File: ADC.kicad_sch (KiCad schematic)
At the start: 32 parts, among them U107 ADR4540, U111 ADA4841-1, U97 AD7768

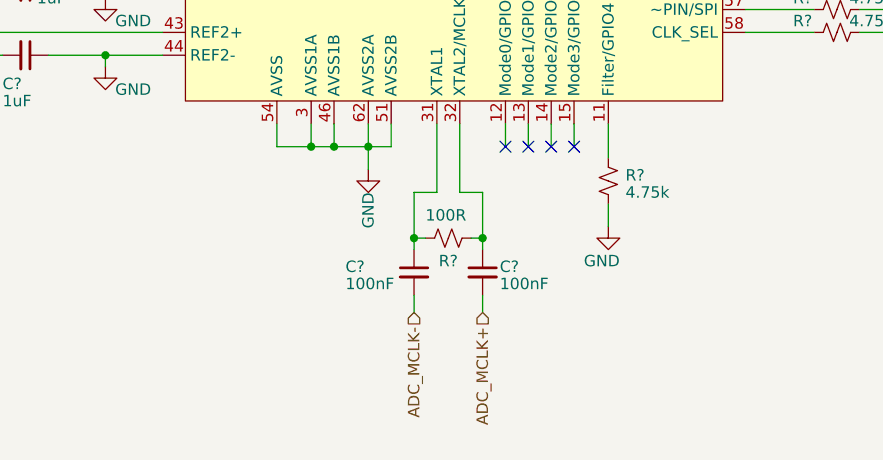
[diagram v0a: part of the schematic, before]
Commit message: Updating design to cover reworks
Updating design to cover reworks.
This should now match what has been delivered to NASA GRE-ATF after the board reworks.
All outputs have been regenerated
Changes are:
1)Changed the clock splitter part to a 2.5V compatible part
2)Changed some caps on the MCLK lines to 0R resitors
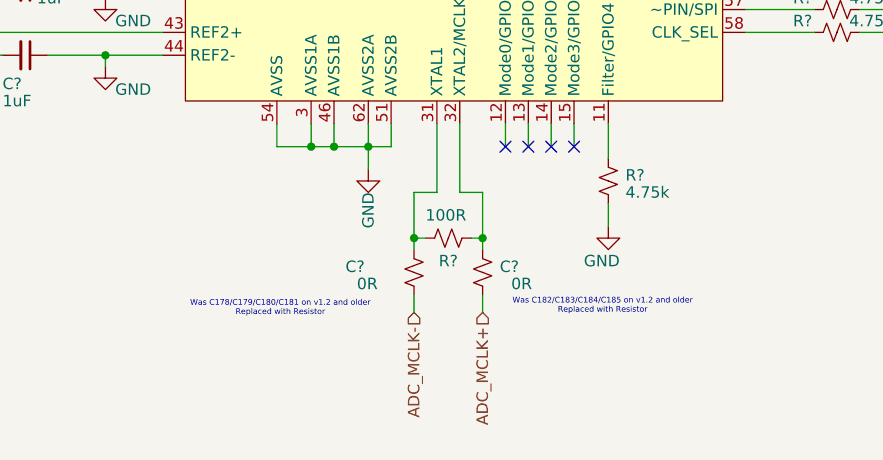
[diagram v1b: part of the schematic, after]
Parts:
- C? (x2): value 100nF -> 0R; footprint Capacitor_SMD:C_0402_1005Metric -> Resistor_SMD:R_0603_1608Metric; symbol Device:C_Small -> Device:R_Small_US; MPN CL05A104KA5NNNC -> ERJ-2GE0R00X
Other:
- note added: "Was C178/C179/C180/C181 on v1.2 and older Replaced with Resistor"
- note added: "Was C182/C183/C184/C185 on v1.2 and older Replaced with Resistor"
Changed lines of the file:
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@@
 		)
 	)
+	(text "Was C178/C179/C180/C181 on v1.2 and older\nReplaced with Resistor"
+		(exclude_from_sim no)
+		(at 158.496 148.844 0)
+		(effects
+			(font
+				(size 0.635 0.635)
+			)
+		)
+	)
 	(text "+2.5V"
 		(exclude_from_sim no)
@@
 		)
 	)
+	(text "Was C182/C183/C184/C185 on v1.2 and older\nReplaced with Resistor"
+		(exclude_from_sim no)
+		(at 194.31 148.59 0)
+		(effects
+			(font
+				(size 0.635 0.635)
+			)
+		)
+	)
 	(label "DREG_CAP"
 		(at 191.135 33.02 270)
@@
 	)
 	(symbol
-		(lib_id "Device:C_Small")
+		(lib_id "Device:R_Small_US")
 		(at 180.975 144.78 0)
 		(unit 1)
@@
 			)
 		)
-		(property "Value" "100nF"
-			(at 182.88 146.05 0)
+		(property "Value" "0R"
+			(at 184.15 146.05 0)
 			(effects
 				(font
@@
 			)
 		)
-		(property "Footprint" "Capacitor_SMD:C_0402_1005Metric"
+		(property "Footprint" "Resistor_SMD:R_0603_1608Metric"
 			(at 180.975 144.78 0)
 			(effects
@@
 			)
 		)
-		(property "MPN" "CL05A104KA5NNNC"
+		(property "MPN" "ERJ-2GE0R00X"
 			(at 180.975 144.78 0)
 			(effects
@@
 			(project "Quartz_v1p2"
 				(path "/674e1e7f-67ba-4e85-a926-dcd5f6a22021/5f1dcf7b-1f0d-41af-8f43-a794235a096a"
-					(reference "C184")
+					(reference "R184")
 					(unit 1)
 				)
 				(path "/674e1e7f-67ba-4e85-a926-dcd5f6a22021/763a2dc6-a957-486b-a6c0-eb0ccf305601"
-					(reference "C183")
+					(reference "R183")
 					(unit 1)
 				)
 				(path "/674e1e7f-67ba-4e85-a926-dcd5f6a22021/7c049f6e-eb60-47dd-be1c-e0af8d8a491e"
-					(reference "C185")
+					(reference "R185")
 					(unit 1)
 				)
 				(path "/674e1e7f-67ba-4e85-a926-dcd5f6a22021/c1293333-1878-4cba-a3bd-0c7884de1f1a"
-					(reference "C182")
+					(reference "R182")
 					(unit 1)
 				)
@@
 	)
 	(symbol
-		(lib_id "Device:C_Small")
+		(lib_id "Device:R_Small_US")
 		(at 173.355 144.78 0)
 		(unit 1)
@@
 			)
 		)
-		(property "Value" "100nF"
-			(at 165.735 146.05 0)
+		(property "Value" "0R"
+			(at 167.005 146.05 0)
 			(effects
 				(font
@@
 			)
 		)
-		(property "Footprint" "Capacitor_SMD:C_0402_1005Metric"
+		(property "Footprint" "Resistor_SMD:R_0603_1608Metric"
 			(at 173.355 144.78 0)
 			(effects
@@
 			)
 		)
-		(property "MPN" "CL05A104KA5NNNC"
+		(property "MPN" "ERJ-2GE0R00X"
 			(at 173.355 144.78 0)
 			(effects
@@
 			(project "Quartz_v1p2"
 				(path "/674e1e7f-67ba-4e85-a926-dcd5f6a22021/5f1dcf7b-1f0d-41af-8f43-a794235a096a"
-					(reference "C180")
+					(reference "R180")
 					(unit 1)
 				)
 				(path "/674e1e7f-67ba-4e85-a926-dcd5f6a22021/763a2dc6-a957-486b-a6c0-eb0ccf305601"
-					(reference "C179")
+					(reference "R179")
 					(unit 1)
 				)
 				(path "/674e1e7f-67ba-4e85-a926-dcd5f6a22021/7c049f6e-eb60-47dd-be1c-e0af8d8a491e"
-					(reference "C181")
+					(reference "R181")
 					(unit 1)
 				)
 				(path "/674e1e7f-67ba-4e85-a926-dcd5f6a22021/c1293333-1878-4cba-a3bd-0c7884de1f1a"
-					(reference "C178")
+					(reference "R178")
 					(unit 1)
 				)

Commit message: Opened & Saved Project in Kicad 9
- Opened & Saved Project in Kicad 9
- Added .gitignore from main
- Added sym-lib-table to link the unchanged symbol libs to the project
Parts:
- gave numbers to parts that had none: 29
- renumbered U97 to U1, U107 to U2, U111 to U3

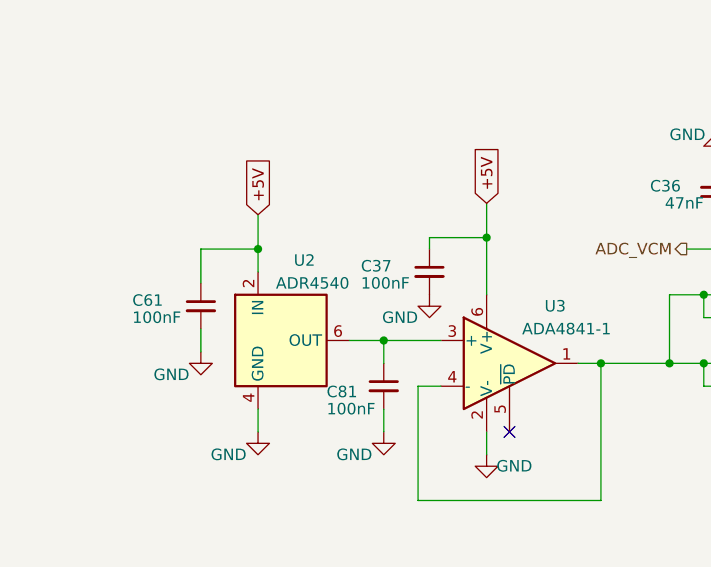
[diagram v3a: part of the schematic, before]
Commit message: Verified 'Must do changes' implemented all 'should do' changes
Must do Changes that have been verified:
-Change the Clock divider chip to the 2,5V part
-Remove AC coupling caps in clock lines

Should do changes implmented
  - Add pull up resistor to ADC reset lines
  - Internal termination of PPS (when unused)
  - Add Heat Sinking to inductors by increased traces/planes size (Copied/Based-On from V2 Design)
  - Changed to a 2.048V VREF with accompanying removal of INA851 gain resistor (this will give more dynamic range)
  - Move ground test points further away from power rails

Also Included Some Improvments to the power rails seen in V2 when in comes to:
-12V rail into the power section and up to the front of the board
-The 3.3V rail that goes around the edge of the board to the relay switch IC's

Note - DRC warnings that exist are either ignorable, or pointing to the fact that the default footprint libs may have been changed in Kicad9 causeing a mismatch to what is on the board. I will no update these footprint to the new version yet, or possibly ever.
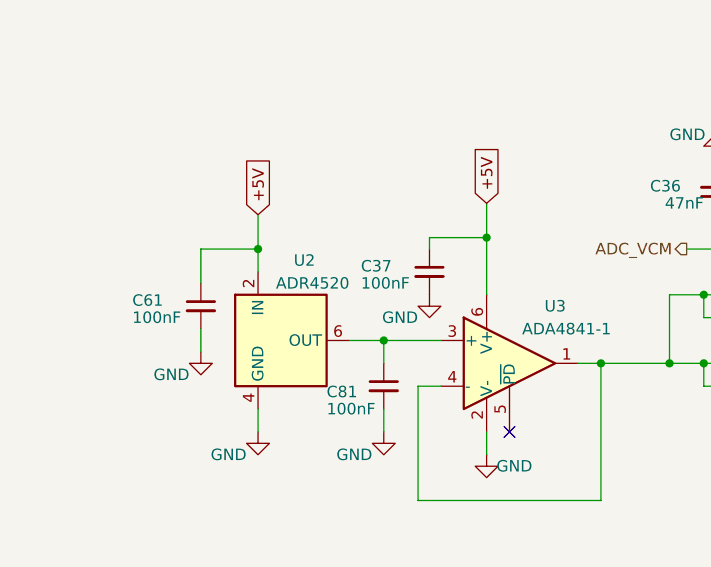
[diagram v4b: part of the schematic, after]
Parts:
- U2: value ADR4540 -> ADR4520; MPN ADR4540BRZ -> ADR4520BRZ
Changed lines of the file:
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@@
 			)
 		)
-		(property "Value" "ADR4540"
+		(property "Value" "ADR4520"
 			(at 85.725 109.22 0)
 			(effects
@@
 			)
 		)
-		(property "MPN" "ADR4540BRZ"
+		(property "MPN" "ADR4520BRZ"
 			(at 78.105 115.57 0)
 			(effects
